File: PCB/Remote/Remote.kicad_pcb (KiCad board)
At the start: 2 copper layers, 70 x 70 mm, 50 parts, among them J1 LCD, J2 DC, J3 TEMP, J4 LCD, J5 Reset, J6 USB-C-Socket-H, J7 TC2030-USB-NL-DS, T1 T3902_MEMS_Mic, U1 ESP32-S3-MINI-1, U2 SCD41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

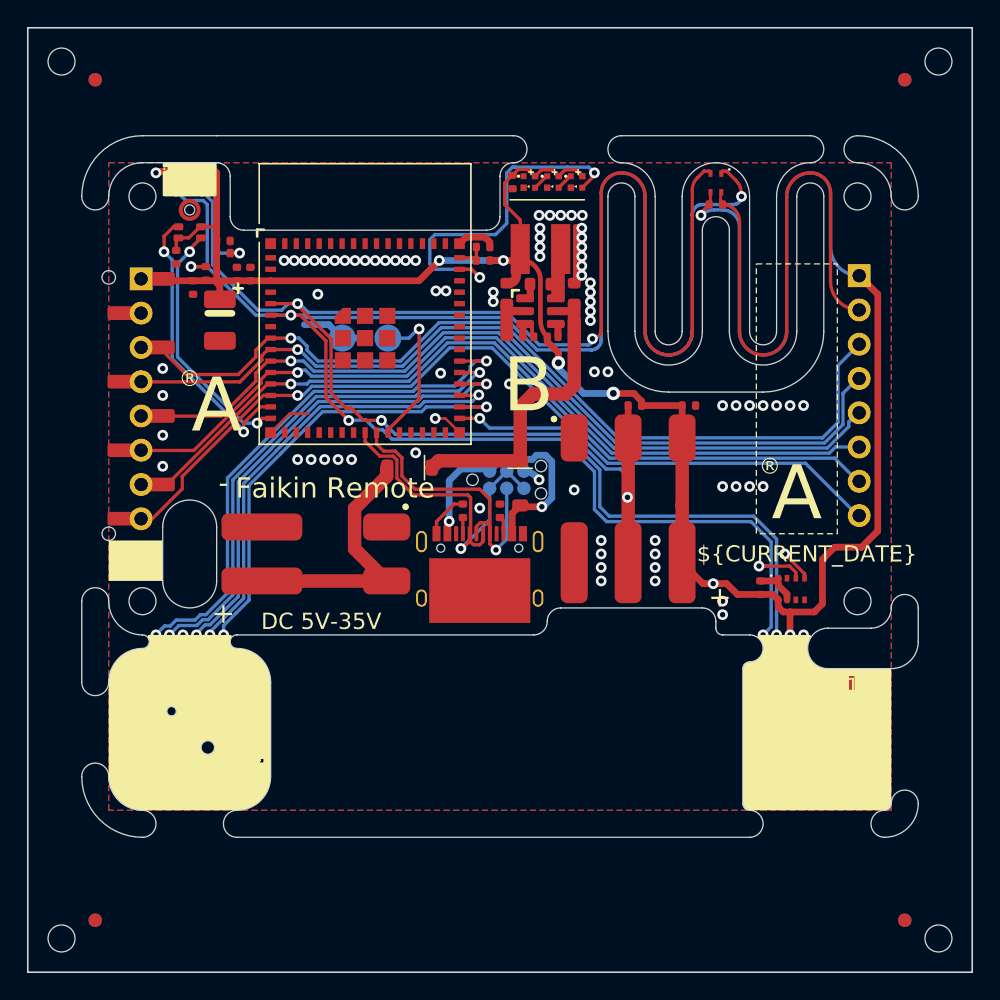
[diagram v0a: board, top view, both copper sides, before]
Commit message: Reworked for connecting switch/SCD41
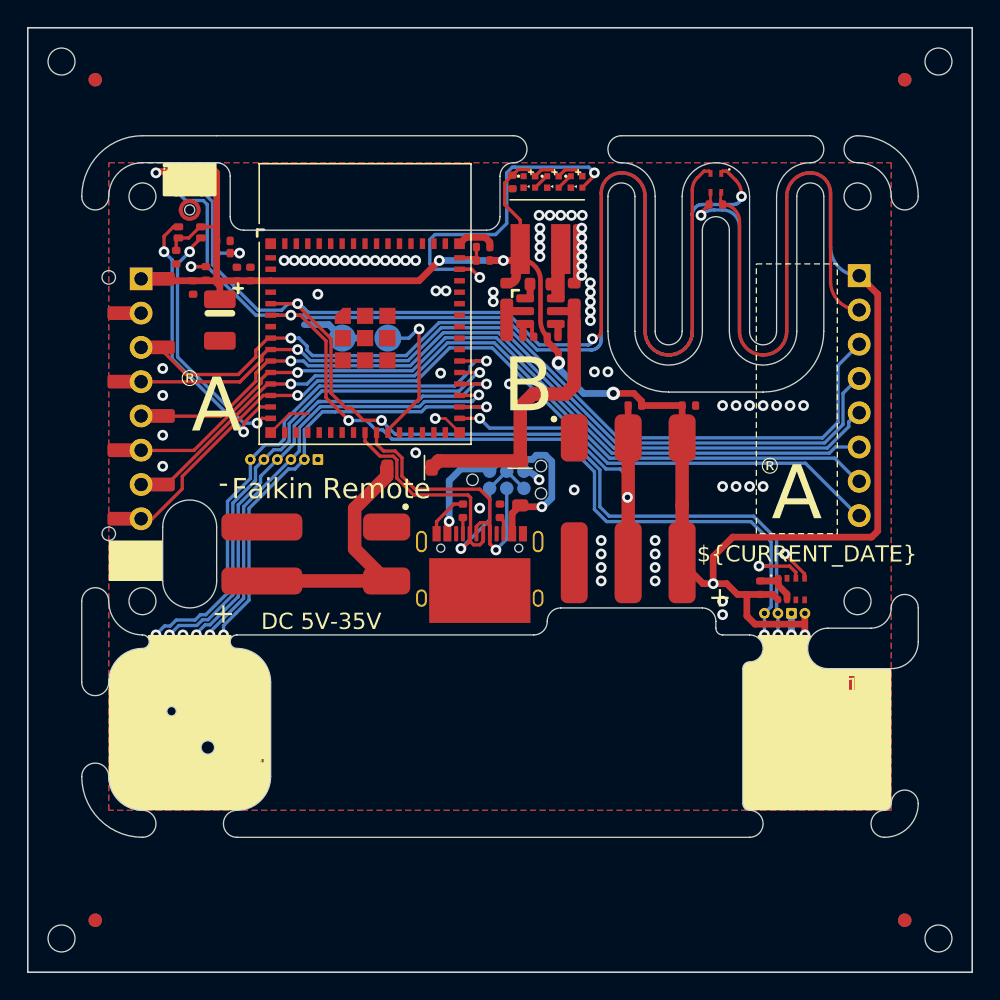
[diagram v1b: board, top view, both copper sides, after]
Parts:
- added TP1: TestPoint, RevK:TestPad, F.Cu at (85.5, 97.0)
- added TP10: TestPoint, RevK:TestPad, F.Cu at (82.0, 115.5)
- added TP11: TestPoint, RevK:TestPad, F.Cu at (82.0, 114.5)
- added TP12: TestPoint, RevK:TestPadSquare, F.Cu at (82.0, 119.5)
- added TP13: TestPoint, RevK:TestPad, F.Cu at (119.6, 108.4)
- added TP14: TestPoint, RevK:TestPad, F.Cu at (120.6, 108.4)
- added TP15: TestPoint, RevK:TestPad, F.Cu at (122.6, 108.4)
- added TP16: TestPoint, RevK:TestPadSquare, F.Cu at (121.6, 108.4)
- added TP17: TestPoint, RevK:TestPad, F.Cu at (119.6, 112.2)
- added TP18: TestPoint, RevK:TestPad, F.Cu at (120.6, 112.2)
- added TP19: TestPoint, RevK:TestPad, F.Cu at (122.6, 112.2)
- added TP2: TestPoint, RevK:TestPad, F.Cu at (84.5, 97.0)
- added TP20: TestPoint, RevK:TestPadSquare, F.Cu at (121.6, 112.2)
- added TP3: TestPoint, RevK:TestPad, F.Cu at (83.5, 97.0)
- added TP4: TestPoint, RevK:TestPad, F.Cu at (82.5, 97.0)
- added TP5: TestPoint, RevK:TestPad, F.Cu at (81.5, 97.0)
- added TP6: TestPoint, RevK:TestPadSquare, F.Cu at (86.5, 97.0)
- added TP7: TestPoint, RevK:TestPad, F.Cu at (82.0, 118.5)
- added TP8: TestPoint, RevK:TestPad, F.Cu at (82.0, 117.5)
- added TP9: TestPoint, RevK:TestPad, F.Cu at (82.0, 116.5)
- moved C5 0.30 mm to (121.8, 111.0), turned to 180 degrees
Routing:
- net P: track 49.2 -> 61.7 mm
- net W: track 53.0 -> 62.2 mm, vias 2 -> 3
- net N: track 48.3 -> 57.0 mm
- net E: track 42.4 -> 49.3 mm, vias 2 -> 3
- net +3.3V: track 191.5 -> 197.4 mm
- net GND: track 79.8 -> 84.7 mm, vias 89 -> 85
- net S: track 44.3 -> 45.7 mm
- net SDA: track 161.8 -> 162.8 mm
- net SCL: track 153.4 -> 154.1 mm

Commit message: New rendere
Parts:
- added C13: 4.7uF, RevK:C_0402, F.Cu at (87.1, 114.7)
- added D10: ~, RevK:DFN1006-2L, F.Cu at (72.0, 115.5)
- added D11: ~, RevK:DFN1006-2L, F.Cu at (107.0, 93.0)
- added D12: ~, RevK:DFN1006-2L, F.Cu at (90.5, 113.0)
- added D13: ~, RevK:DFN1006-2L, F.Cu at (123.5, 104.5)
- added D14: ~, RevK:DFN1006-2L, F.Cu at (124.5, 104.5)
- added D3: ~, RevK:DFN1006-2L, F.Cu at (74.0, 122.0)
- added D7: ~, RevK:DFN1006-2L, F.Cu at (72.0, 120.0)
- added D8: ~, RevK:DFN1006-2L, F.Cu at (80.0, 122.0)
- added D9: ~, RevK:DFN1006-2L, F.Cu at (77.0, 111.5)
- added R9: 100R, RevK:R_0402, F.Cu at (89.1, 114.7)
- added TP21: TestPoint, RevK:TestPad, F.Cu at (88.0, 113.0)
- added TP22: TestPoint, RevK:TestPadSquare, F.Cu at (88.0, 97.0)
- added TP23: TestPoint, RevK:TestPad, F.Cu at (89.0, 113.0)
- added TP24: TestPoint, RevK:TestPad, F.Cu at (89.0, 97.0)
- added TP25: TestPoint, RevK:TestPadSquare, F.Cu at (87.0, 113.0)
- added TP26: TestPoint, RevK:TestPad, F.Cu at (90.0, 97.0)
- added U6: IRM-H638T/TR2, RevK:SMD-4P,4x5mm, F.Cu at (88.0, 117.9)
- R6, R7: value 10K -> 4k7
- moved R7 4.33 mm to (81.0, 86.5), turned to 0 degrees
- moved R6 4.09 mm to (81.0, 85.5)
- moved C7 0.75 mm to (76.5, 84.2)
- moved C4 0.74 mm to (78.5, 86.7)
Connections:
- U1 pad 22: unconnected-(U1-GPIO18-Pad22) -> IR
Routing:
- net +3.3V: track 197.4 -> 245.6 mm, vias 8 -> 9
- net GND: track 84.7 -> 128.5 mm, vias 85 -> 89
- net IR: track 0.00 -> 28.5 mm, vias 0 -> 1
- net S: track 45.7 -> 54.5 mm, vias 2 -> 3
- net Net-(U6-VCC): track 0.00 -> 4.10 mm
- net SDA: track 162.8 -> 165.8 mm, vias 8 -> 7
- net W: track 62.2 -> 64.3 mm
- net TEMP: track 27.4 -> 29.4 mm
- net VDC: track 20.2 -> 18.8 mm
- net N: track 57.0 -> 57.8 mm
- net SCL: vias 7 -> 6
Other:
- board text added: "18"
- board text added: "IR"
- board text added: "IR 38kHz"
- board text added: "Switch"

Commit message: Tidy rendering
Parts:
- moved C13 0.25 mm to (86.8, 114.7)
- moved D12 0.25 mm to (90.2, 113.0)
- moved R9 0.25 mm to (88.8, 114.7)
- moved TP21 0.25 mm to (87.8, 113.0)
- moved TP23 0.25 mm to (88.8, 113.0)
- moved TP25 0.25 mm to (86.8, 113.0)
- moved U6 0.25 mm to (87.8, 117.9)

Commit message: Tweak
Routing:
- net GND: vias 89 -> 90

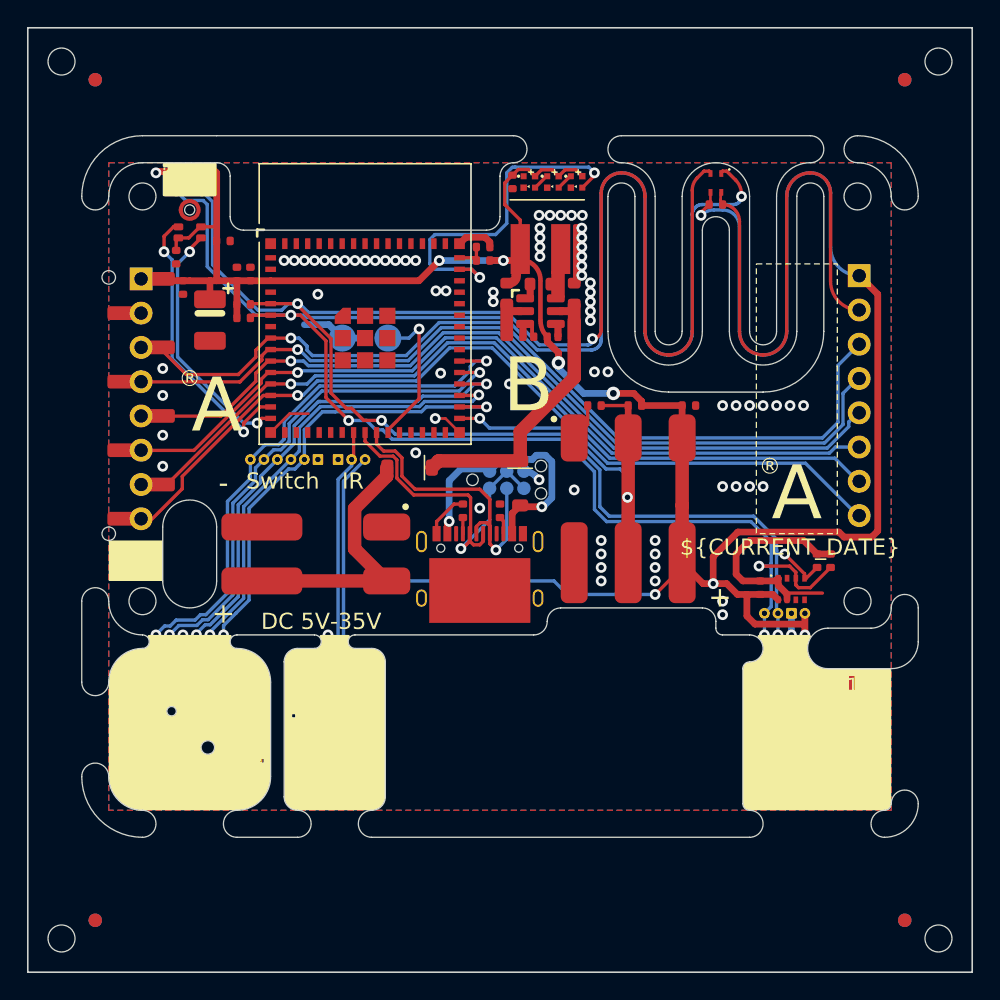
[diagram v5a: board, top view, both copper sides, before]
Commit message: Better clearance on USB lead
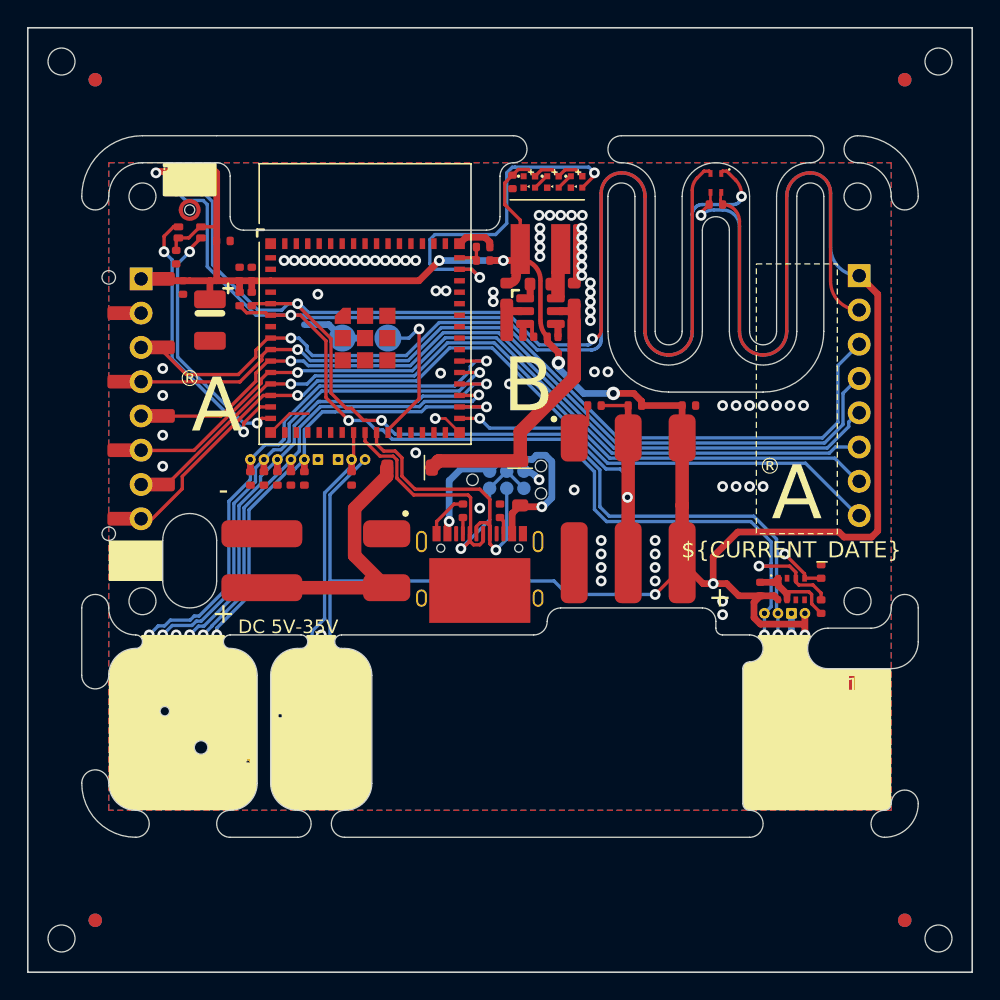
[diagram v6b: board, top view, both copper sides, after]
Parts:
- moved D3 26.3 mm to (85.5, 98.4), turned to -90 degrees
- moved D7 25.0 mm to (84.5, 98.4)
- moved D8 23.9 mm to (83.5, 98.4), turned to -90 degrees
- moved D10 19.6 mm to (81.5, 98.4), turned to -90 degrees
- moved D12 14.7 mm to (89.0, 98.4)
- moved D9 14.2 mm to (82.5, 98.4), turned to -90 degrees
- moved D14 3.47 mm to (123.8, 107.9), turned to 90 degrees
- moved R7 1.43 mm to (80.7, 85.1), turned to -90 degrees
- moved C13 1.00 mm to (85.8, 114.7)
- moved R9 1.00 mm to (87.8, 114.7)
- moved TP21 1.00 mm to (86.8, 113.0)
- moved TP23 1.00 mm to (87.8, 113.0)
- moved TP25 1.00 mm to (85.8, 113.0)
- moved U6 1.00 mm to (86.8, 117.9)
- moved D13 0.85 mm to (123.8, 105.3)
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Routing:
- net GND: track 128.5 -> 93.5 mm
- net S: track 54.5 -> 46.5 mm, vias 3 -> 2
- net W: track 64.3 -> 60.3 mm
- net P: track 61.7 -> 58.8 mm
- net IR: track 28.5 -> 27.6 mm
- net E: track 49.3 -> 50.0 mm
- net Net-(D19-A): track 19.6 -> 20.1 mm
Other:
- board text removed: "IR"
- board text removed: "Switch"

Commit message: Library update
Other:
- board text added: "5V-35V"
- board text removed: "DC 5V-35V"

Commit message: Moved around
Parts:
- moved TP12 7.83 mm to (79.0, 112.0), turned to 0 degrees
- moved TP11 7.67 mm to (74.0, 112.0), turned to 0 degrees
- moved TP7 7.27 mm to (78.0, 112.0), turned to 0 degrees
- moved TP10 7.16 mm to (75.0, 112.0), turned to 0 degrees
- moved TP8 6.95 mm to (77.0, 112.0), turned to 0 degrees
- moved TP9 6.91 mm to (76.0, 112.0), turned to 0 degrees
- moved C13 1.70 mm to (85.8, 113.0)
- moved R9 1.70 mm to (87.8, 113.0)
- moved TP21 1.00 mm to (86.8, 112.0)
- moved TP23 1.00 mm to (87.8, 112.0)
- moved TP25 1.00 mm to (85.8, 112.0)
- moved SW1 0.50 mm to (76.5, 117.5)
- moved U6 0.40 mm to (86.8, 117.5), turned to -90 degrees
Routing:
- net N: track 58.0 -> 46.7 mm, vias 3 -> 2
- net P: track 58.8 -> 47.9 mm, vias 3 -> 2
- net Net-(U6-VCC): track 3.73 -> 8.72 mm
- net W: track 60.3 -> 55.6 mm, vias 3 -> 2
- net S: track 46.5 -> 48.7 mm, vias 2 -> 3
- net IR: track 27.6 -> 29.4 mm
- net +3.3V: track 245.5 -> 243.7 mm
- net GND: track 93.5 -> 94.9 mm, vias 90 -> 83
- net E: track 50.0 -> 48.8 mm
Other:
- board text added: "T3902 (R)"
- board text removed: "T3902 (L)"
